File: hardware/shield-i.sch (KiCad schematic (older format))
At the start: 11 parts, among them J201 Fan2, J202 Endstop, J203 Conn_01x10_Female, J204 Conn_01x10_Female, Q201 IRLR7843PbF

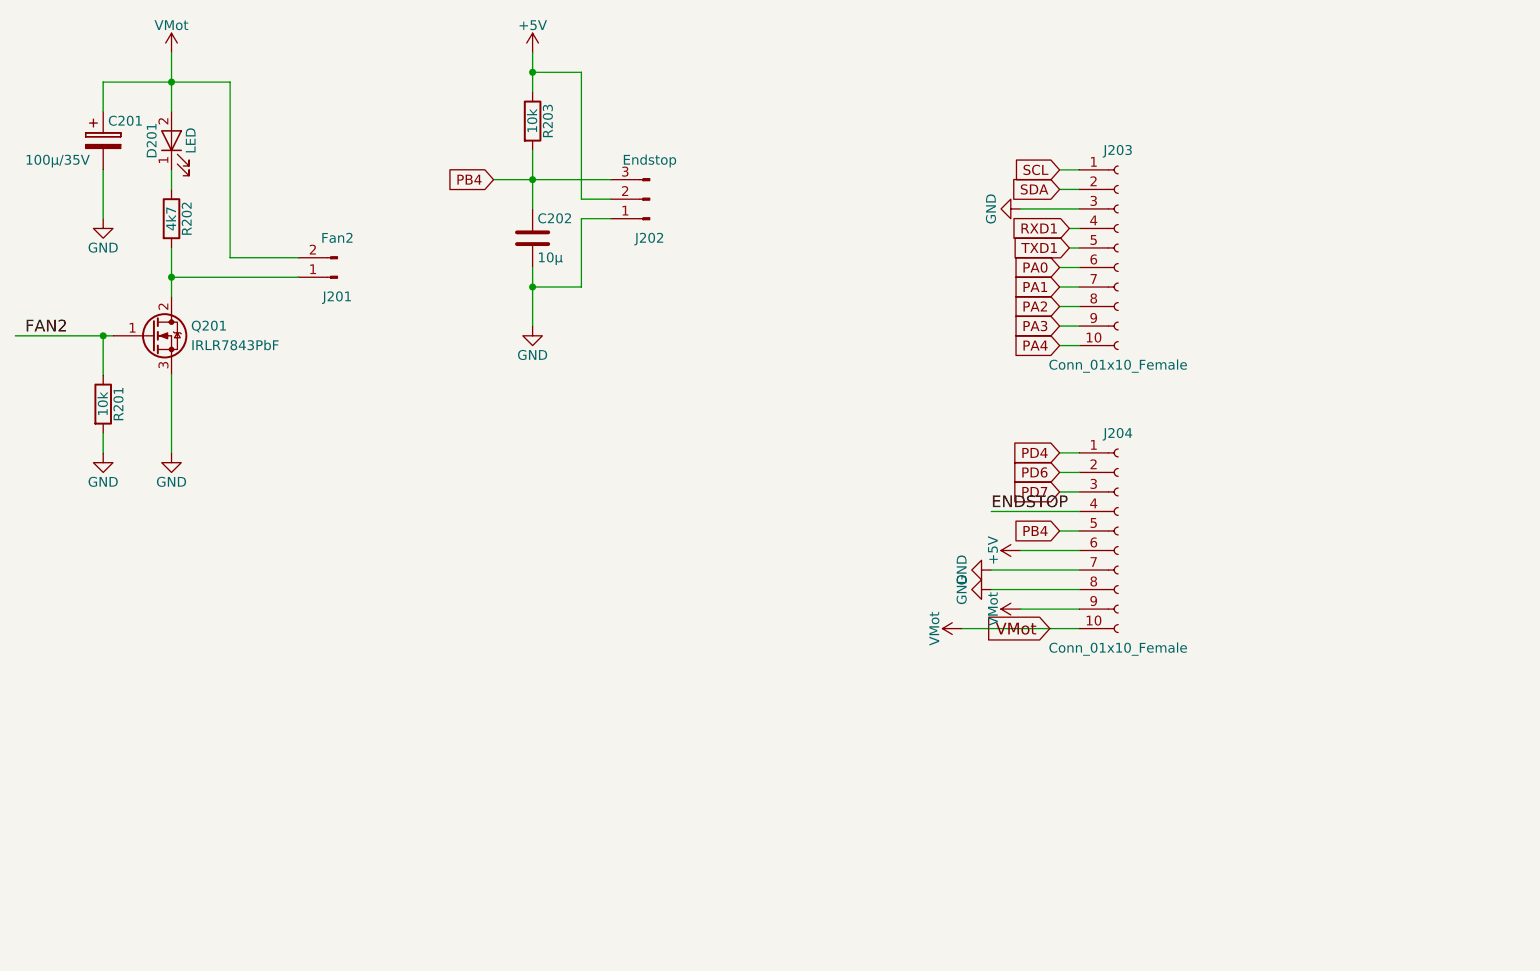
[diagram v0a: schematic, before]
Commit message: Components positioned
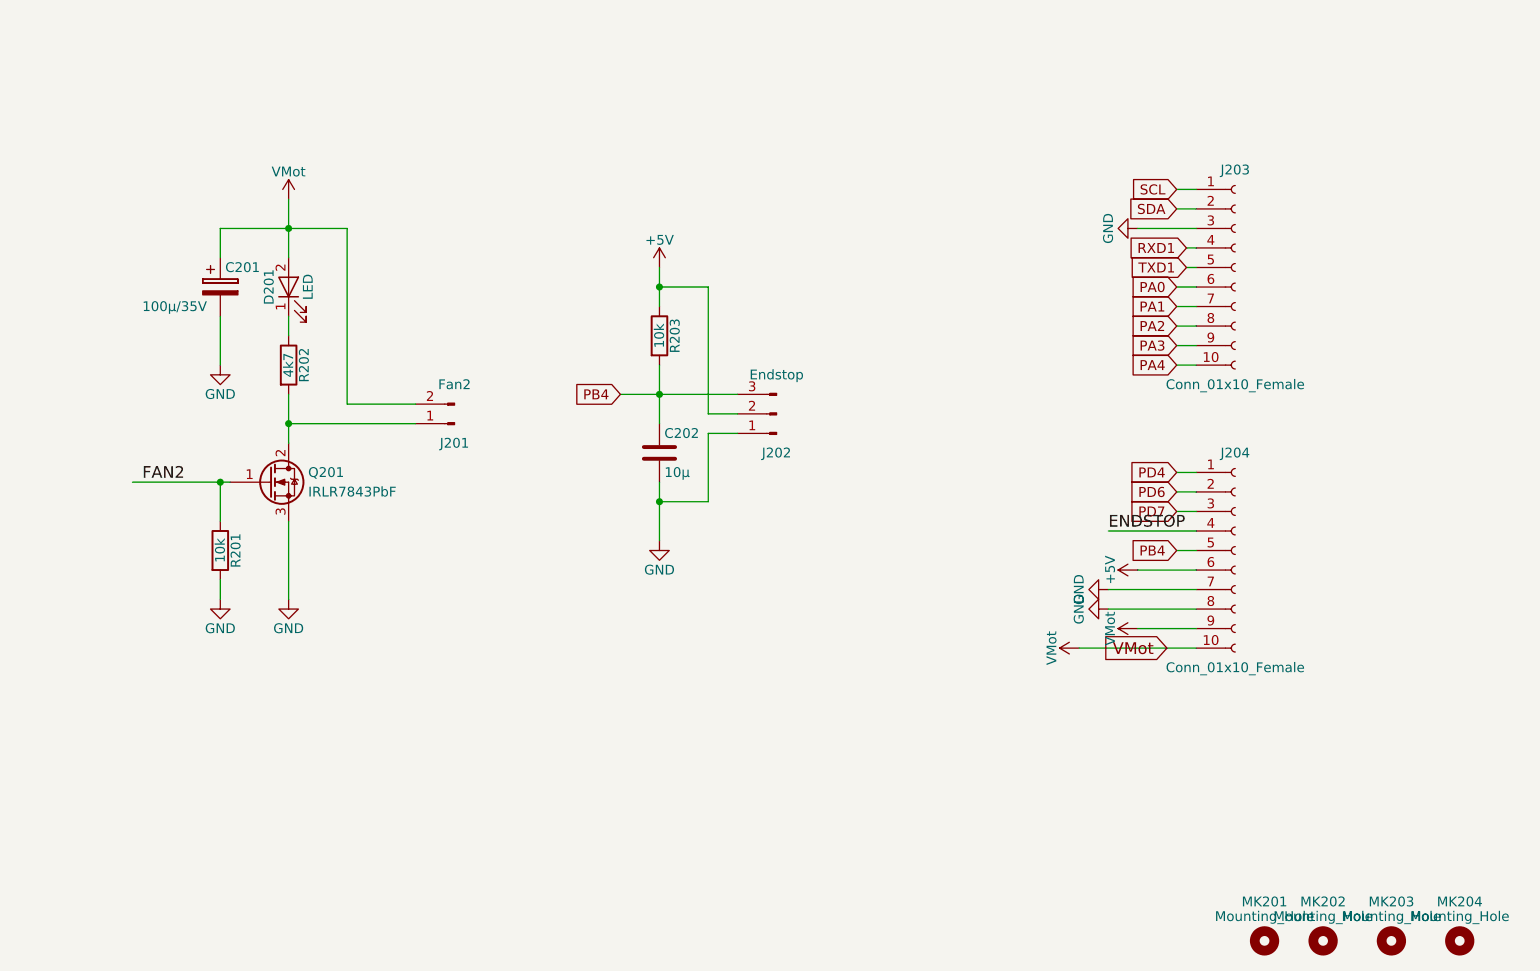
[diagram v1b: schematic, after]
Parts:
- added MK201, MK202, MK203, MK204: Mounting_Hole, Mounting_Holes:MountingHole_3mm, symbol Mounting_Hole
- C202: footprint (none) -> Capacitors_SMD:C_1206_HandSoldering
- J202: footprint (none) -> Connectors_JST:JST_XH_B03B-XH-A_03x2.50mm_Straight
- J203, J204: footprint (none) -> Pin_Headers:Pin_Header_Straight_1x10_Pitch2.54mm
- R203: footprint (none) -> Resistors_SMD:R_1206_HandSoldering
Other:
- moved on the sheet: C201, C202, D201, J201, J202, J203, J204, Q201, R201, R202, R203
